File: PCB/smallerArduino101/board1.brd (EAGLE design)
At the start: 47.9 x 59.7 mm, 41 parts

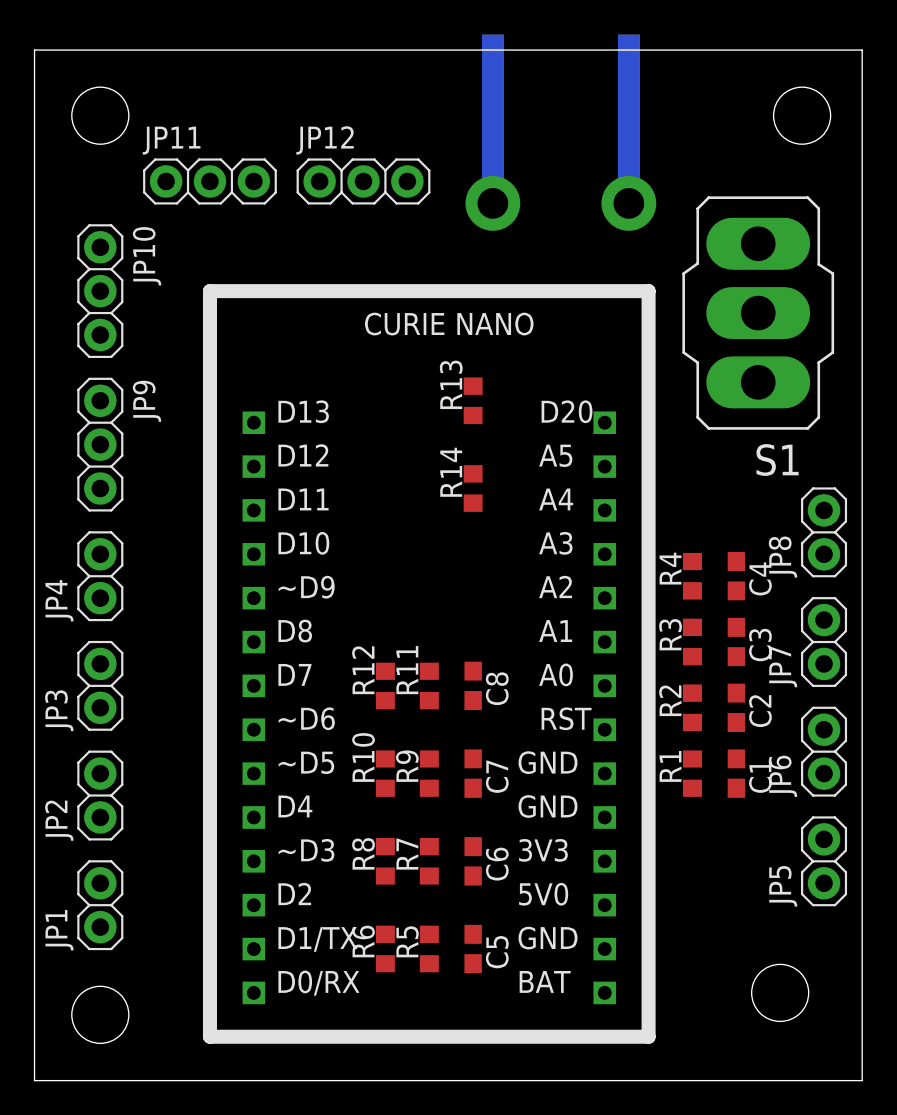
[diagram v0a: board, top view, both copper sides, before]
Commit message: renamed jumpers and connectors
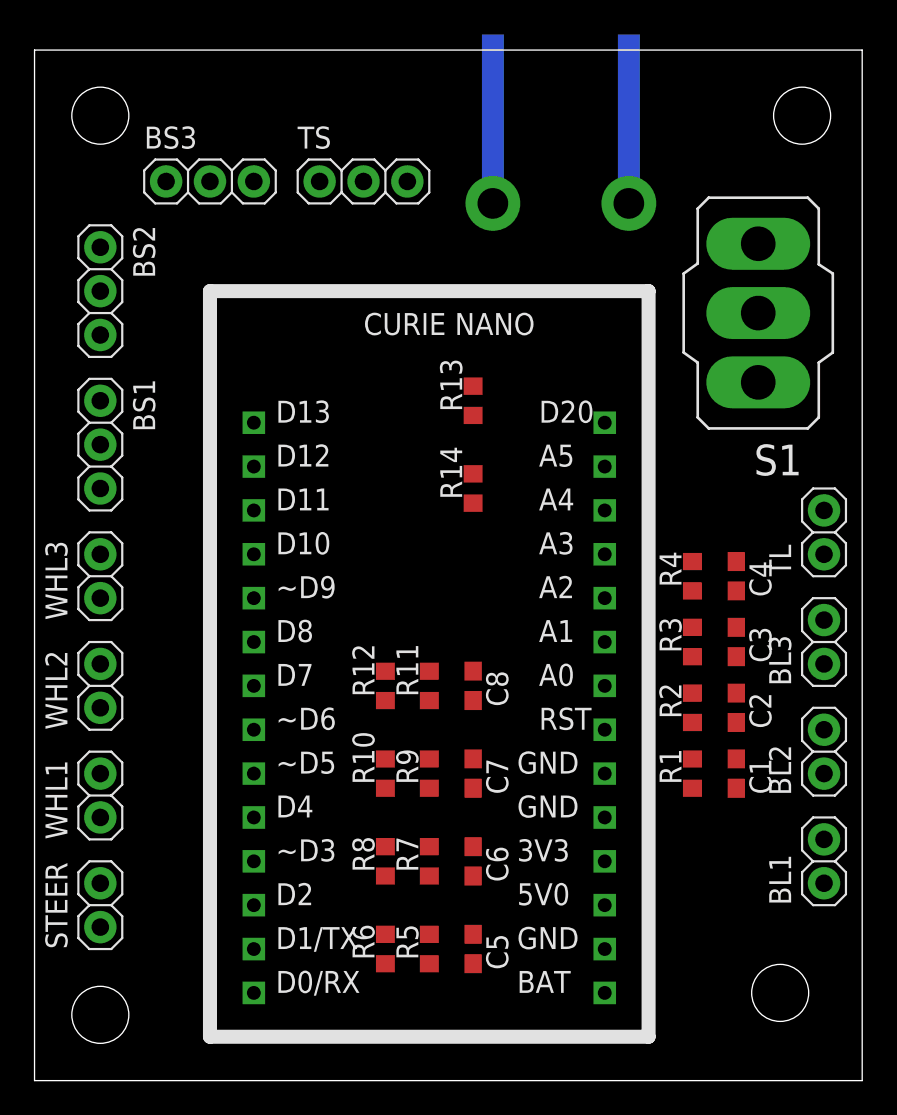
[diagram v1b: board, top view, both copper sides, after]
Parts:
- renumbered CONN1 to 14V8, JP1 to STEER, JP10 to BS2, JP11 to BS3, JP12 to TS, JP2 to WHL1, JP3 to WHL2, JP4 to WHL3, JP5 to BL1, JP6 to BL2, JP7 to BL3, JP8 to TL, JP9 to BS1
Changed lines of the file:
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@@
 <attribute name="NAME" x="46.482" y="23.749" size="1.27" layer="25" rot="R270"/>
 </element>
-<element name="CONN1" library="ee192" package="ANDERSON_HORIZONTAL" value="ANDERSONHORIZONTAL" x="50.8" y="50.8" rot="MR270">
+<element name="14V8" library="ee192" package="ANDERSON_HORIZONTAL" value="ANDERSONHORIZONTAL" x="50.8" y="50.8" rot="MR270">
 <attribute name="PIE-INT-REF-NUM" value="Anderson" x="50.8" y="50.8" size="1.778" layer="28" rot="MR270" display="off"/>
 </element>
-<element name="JP1" library="ee192" package="1X02" value="" x="24.13" y="10.16" rot="R90">
+<element name="STEER" library="ee192" package="1X02" value="" x="24.13" y="10.16" rot="R90">
 <attribute name="PIE-INT-REF-NUM" value="BULK-STOCK" x="24.13" y="10.16" size="1.778" layer="27" rot="R90" display="off"/>
 </element>
-<element name="JP10" library="ee192" package="1X03" value="" x="24.13" y="45.72" rot="R270">
+<element name="BS2" library="ee192" package="1X03" value="" x="24.13" y="45.72" rot="R270">
 <attribute name="PIE-INT-REF-NUM" value="BULK-STOCK" x="24.13" y="45.72" size="1.778" layer="27" rot="R270" display="off"/>
 </element>
-<element name="JP11" library="ee192" package="1X03" value="" x="30.48" y="52.07">
+<element name="BS3" library="ee192" package="1X03" value="" x="30.48" y="52.07">
 <attribute name="PIE-INT-REF-NUM" value="BULK-STOCK" x="30.48" y="52.07" size="1.778" layer="27" display="off"/>
 </element>
-<element name="JP12" library="ee192" package="1X03" value="" x="39.37" y="52.07">
+<element name="TS" library="ee192" package="1X03" value="" x="39.37" y="52.07">
 <attribute name="PIE-INT-REF-NUM" value="BULK-STOCK" x="39.37" y="52.07" size="1.778" layer="27" display="off"/>
 </element>
@@
 <element name="JP15" library="ee192" package="STAND-OFF" value="STAND-OFF" x="24.13" y="55.88"/>
 <element name="JP16" library="ee192" package="STAND-OFF" value="STAND-OFF" x="64.77" y="55.88"/>
-<element name="JP2" library="ee192" package="1X02" value="" x="24.13" y="16.51" rot="R90">
+<element name="WHL1" library="ee192" package="1X02" value="" x="24.13" y="16.51" rot="R90">
 <attribute name="PIE-INT-REF-NUM" value="BULK-STOCK" x="24.13" y="16.51" size="1.778" layer="27" rot="R90" display="off"/>
 </element>
-<element name="JP3" library="ee192" package="1X02" value="" x="24.13" y="22.86" rot="R90">
+<element name="WHL2" library="ee192" package="1X02" value="" x="24.13" y="22.86" rot="R90">
 <attribute name="PIE-INT-REF-NUM" value="BULK-STOCK" x="24.13" y="22.86" size="1.778" layer="27" rot="R90" display="off"/>
 </element>
-<element name="JP4" library="ee192" package="1X02" value="" x="24.13" y="29.21" rot="R90">
+<element name="WHL3" library="ee192" package="1X02" value="" x="24.13" y="29.21" rot="R90">
 <attribute name="PIE-INT-REF-NUM" value="BULK-STOCK" x="24.13" y="29.21" size="1.778" layer="27" rot="R90" display="off"/>
 </element>
-<element name="JP5" library="ee192" package="1X02" value="" x="66.04" y="12.7" rot="R90">
+<element name="BL1" library="ee192" package="1X02" value="" x="66.04" y="12.7" rot="R90">
 <attribute name="PIE-INT-REF-NUM" value="BULK-STOCK" x="66.04" y="12.7" size="1.778" layer="27" rot="R90" display="off"/>
 </element>
-<element name="JP6" library="ee192" package="1X02" value="" x="66.04" y="19.05" rot="R90">
+<element name="BL2" library="ee192" package="1X02" value="" x="66.04" y="19.05" rot="R90">
 <attribute name="PIE-INT-REF-NUM" value="BULK-STOCK" x="66.04" y="19.05" size="1.778" layer="27" rot="R90" display="off"/>
 </element>
-<element name="JP7" library="ee192" package="1X02" value="" x="66.04" y="25.4" rot="R90">
+<element name="BL3" library="ee192" package="1X02" value="" x="66.04" y="25.4" rot="R90">
 <attribute name="PIE-INT-REF-NUM" value="BULK-STOCK" x="66.04" y="25.4" size="1.778" layer="27" rot="R90" display="off"/>
 </element>
-<element name="JP8" library="ee192" package="1X02" value="" x="66.04" y="31.75" rot="R90">
+<element name="TL" library="ee192" package="1X02" value="" x="66.04" y="31.75" rot="R90">
 <attribute name="PIE-INT-REF-NUM" value="BULK-STOCK" x="66.04" y="31.75" size="1.778" layer="27" rot="R90" display="off"/>
 </element>
-<element name="JP9" library="ee192" package="1X03" value="" x="24.13" y="36.83" rot="R270">
+<element name="BS1" library="ee192" package="1X03" value="" x="24.13" y="36.83" rot="R270">
 <attribute name="PIE-INT-REF-NUM" value="BULK-STOCK" x="24.13" y="36.83" size="1.778" layer="27" rot="R270" display="off"/>
 </element>
@@
 <contactref element="R1" pad="2"/>
 <contactref element="C1" pad="1"/>
-<contactref element="JP5" pad="1"/>
+<contactref element="BL1" pad="1"/>
 <wire x1="60.96" y1="18.63" x2="66.04" y2="11.43" width="0" layer="19" extent="1-1"/>
 <wire x1="58.42" y1="18.63" x2="60.96" y2="18.63" width="0" layer="19" extent="1-1"/>
@@
 <contactref element="R2" pad="2"/>
 <contactref element="C2" pad="1"/>
-<contactref element="JP6" pad="1"/>
+<contactref element="BL2" pad="1"/>
 <wire x1="60.96" y1="22.44" x2="66.04" y2="17.78" width="0" layer="19" extent="1-1"/>
 <wire x1="58.42" y1="22.44" x2="60.96" y2="22.44" width="0" layer="19" extent="1-1"/>
@@
 <contactref element="R3" pad="2"/>
 <contactref element="C3" pad="1"/>
-<contactref element="JP7" pad="1"/>
+<contactref element="BL3" pad="1"/>
 <wire x1="60.96" y1="26.25" x2="66.04" y2="24.13" width="0" layer="19" extent="1-1"/>
 <wire x1="58.42" y1="26.25" x2="60.96" y2="26.25" width="0" layer="19" extent="1-1"/>
@@
 <contactref element="R4" pad="2"/>
 <contactref element="C4" pad="1"/>
-<contactref element="JP8" pad="1"/>
+<contactref element="TL" pad="1"/>
 <wire x1="60.96" y1="30.06" x2="66.04" y2="30.48" width="0" layer="19" extent="1-1"/>
 <wire x1="58.42" y1="30.06" x2="60.96" y2="30.06" width="0" layer="19" extent="1-1"/>
@@
 <signal name="TILT_PWM">
 <contactref element="U$1" pad="D12"/>
-<contactref element="JP12" pad="3"/>
+<contactref element="TS" pad="3"/>
 <wire x1="33.02" y1="35.56" x2="41.91" y2="52.07" width="0" layer="19" extent="1-1"/>
 </signal>
 <signal name="BRAKE_PWM3">
 <contactref element="U$1" pad="D11"/>
-<contactref element="JP11" pad="3"/>
+<contactref element="BS3" pad="3"/>
 <wire x1="33.02" y1="52.07" x2="33.02" y2="33.02" width="0" layer="19" extent="1-1"/>
 </signal>
 <signal name="BRAKE_PWM2">
 <contactref element="U$1" pad="D10"/>
-<contactref element="JP10" pad="3"/>
+<contactref element="BS2" pad="3"/>
 <wire x1="24.13" y1="43.18" x2="33.02" y2="30.48" width="0" layer="19" extent="1-1"/>
 </signal>
 <signal name="BRAKE_PWM1">
 <contactref element="U$1" pad="~D9"/>
-<contactref element="JP9" pad="3"/>
+<contactref element="BS1" pad="3"/>
 <wire x1="24.13" y1="34.29" x2="33.02" y2="27.94" width="0" layer="19" extent="1-1"/>
 </signal>
@@
 <contactref element="R11" pad="1"/>
 <contactref element="C8" pad="2"/>
-<contactref element="JP9" pad="2"/>
-<contactref element="JP10" pad="2"/>
-<contactref element="JP11" pad="2"/>
-<contactref element="JP12" pad="2"/>
+<contactref element="BS1" pad="2"/>
+<contactref element="BS2" pad="2"/>
+<contactref element="BS3" pad="2"/>
+<contactref element="TS" pad="2"/>
 <contactref element="R14" pad="1"/>
-<contactref element="CONN1" pad="PIN1"/>
-<contactref element="CONN1" pad="PIN1-LEAD"/>
+<contactref element="14V8" pad="PIN1"/>
+<contactref element="14V8" pad="PIN1-LEAD"/>
 <wire x1="60.96" y1="24.55" x2="60.96" y2="28.36" width="0" layer="19" extent="1-1"/>
 <wire x1="58.42" y1="28.36" x2="60.96" y2="28.36" width="0" layer="19" extent="1-1"/>
@@
 <signal name="3V3">
 <contactref element="U$1" pad="3V3"/>
-<contactref element="JP1" pad="2"/>
-<contactref element="JP2" pad="2"/>
-<contactref element="JP3" pad="2"/>
-<contactref element="JP4" pad="2"/>
-<contactref element="JP5" pad="2"/>
-<contactref element="JP6" pad="2"/>
-<contactref element="JP7" pad="2"/>
-<contactref element="JP8" pad="2"/>
+<contactref element="STEER" pad="2"/>
+<contactref element="WHL1" pad="2"/>
+<contactref element="WHL2" pad="2"/>
+<contactref element="WHL3" pad="2"/>
+<contactref element="BL1" pad="2"/>
+<contactref element="BL2" pad="2"/>
+<contactref element="BL3" pad="2"/>
+<contactref element="TL" pad="2"/>
 <wire x1="66.04" y1="26.67" x2="66.04" y2="33.02" width="0" layer="19" extent="1-1"/>
 <wire x1="66.04" y1="20.32" x2="66.04" y2="26.67" width="0" layer="19" extent="1-1"/>
@@
 </signal>
 <signal name="N$1">
-<contactref element="JP1" pad="1"/>
+<contactref element="STEER" pad="1"/>
 <contactref element="R6" pad="2"/>
 <wire x1="24.13" y1="8.89" x2="40.64" y2="8.47" width="0" layer="19" extent="1-1"/>
 </signal>
 <signal name="N$2">
-<contactref element="JP2" pad="1"/>
+<contactref element="WHL1" pad="1"/>
 <contactref element="R8" pad="2"/>
 <wire x1="24.13" y1="15.24" x2="40.64" y2="13.55" width="0" layer="19" extent="1-1"/>
 </signal>
 <signal name="N$3">
-<contactref element="JP3" pad="1"/>
+<contactref element="WHL2" pad="1"/>
 <contactref element="R10" pad="2"/>
 <wire x1="24.13" y1="21.59" x2="40.64" y2="18.63" width="0" layer="19" extent="1-1"/>
 </signal>
 <signal name="N$4">
-<contactref element="JP4" pad="1"/>
+<contactref element="WHL3" pad="1"/>
 <contactref element="R12" pad="2"/>
 <wire x1="24.13" y1="27.94" x2="40.64" y2="23.71" width="0" layer="19" extent="1-1"/>
 </signal>
 <signal name="14V8">
-<contactref element="JP9" pad="1"/>
-<contactref element="JP10" pad="1"/>
-<contactref element="JP11" pad="1"/>
-<contactref element="JP12" pad="1"/>
+<contactref element="BS1" pad="1"/>
+<contactref element="BS2" pad="1"/>
+<contactref element="BS3" pad="1"/>
+<contactref element="TS" pad="1"/>
 <contactref element="R13" pad="2"/>
 <contactref element="S1" pad="1"/>
@@
 </signal>
 <signal name="N$5">
-<contactref element="CONN1" pad="PIN2"/>
-<contactref element="CONN1" pad="PIN2-LEAD"/>
+<contactref element="14V8" pad="PIN2"/>
+<contactref element="14V8" pad="PIN2-LEAD"/>
 <contactref element="S1" pad="2"/>
 <wire x1="54.737" y1="50.8" x2="62.23" y2="44.45" width="0" layer="19" extent="1-1"/>

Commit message: added  buck converter
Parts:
- added 3V7: (no value), ee192:1X02
- added LIPO: ANDERSONHORIZONTAL, ee192:ANDERSON_HORIZONTAL
- 14V8: value ANDERSONHORIZONTAL -> (none); device ee192:ANDERSON_HORIZONTAL -> ee192:1X02
- moved 14V8 21.6 mm to (66.0, 35.6), flipped to the top, turned to 90 degrees
- moved JP14 2.84 mm to (61.0, 3.81)
- moved BL1 2.54 mm to (66.0, 10.2)
- moved BL2 2.54 mm to (66.0, 16.5)
- moved BL3 2.54 mm to (66.0, 22.9)
- moved TL 2.54 mm to (66.0, 29.2)
- moved S1 1.27 mm to (62.2, 45.7)
- turned BS3 to 180 degrees
- turned TS to 180 degrees
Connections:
- net 14V8: now also 14V8.2
- net 3V7: now also 3V7.2
- net GND: now also 14V8.1, 3V7.1, LIPO.PIN1, LIPO.PIN1-LEAD; no longer 14V8.PIN1, 14V8.PIN1-LEAD
- net N$5: now also LIPO.PIN2, LIPO.PIN2-LEAD; no longer 14V8.PIN2, 14V8.PIN2-LEAD
